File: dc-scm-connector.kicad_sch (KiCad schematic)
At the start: 10 parts, among them J1 Socket_Amphenol_ME10168134011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

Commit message: [#93514] Propagate title and date across all of the sheets
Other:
- title: DC-SCM Carrier Card for OSM-L SoMs -> Datacenter Secure Control Module Breakout Board
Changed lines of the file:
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@@
 	(paper "A3")
 	(title_block
-		(title "DC-SCM Carrier Card for OSM-L SoMs")
-		(date "2025-10-14")
-		(rev "1.1.0")
+		(title "Datacenter Secure Control Module Breakout Board")
+		(date "2021-12-16")
+		(rev "2.0.0")
 	)
 	(bus_alias "DP"

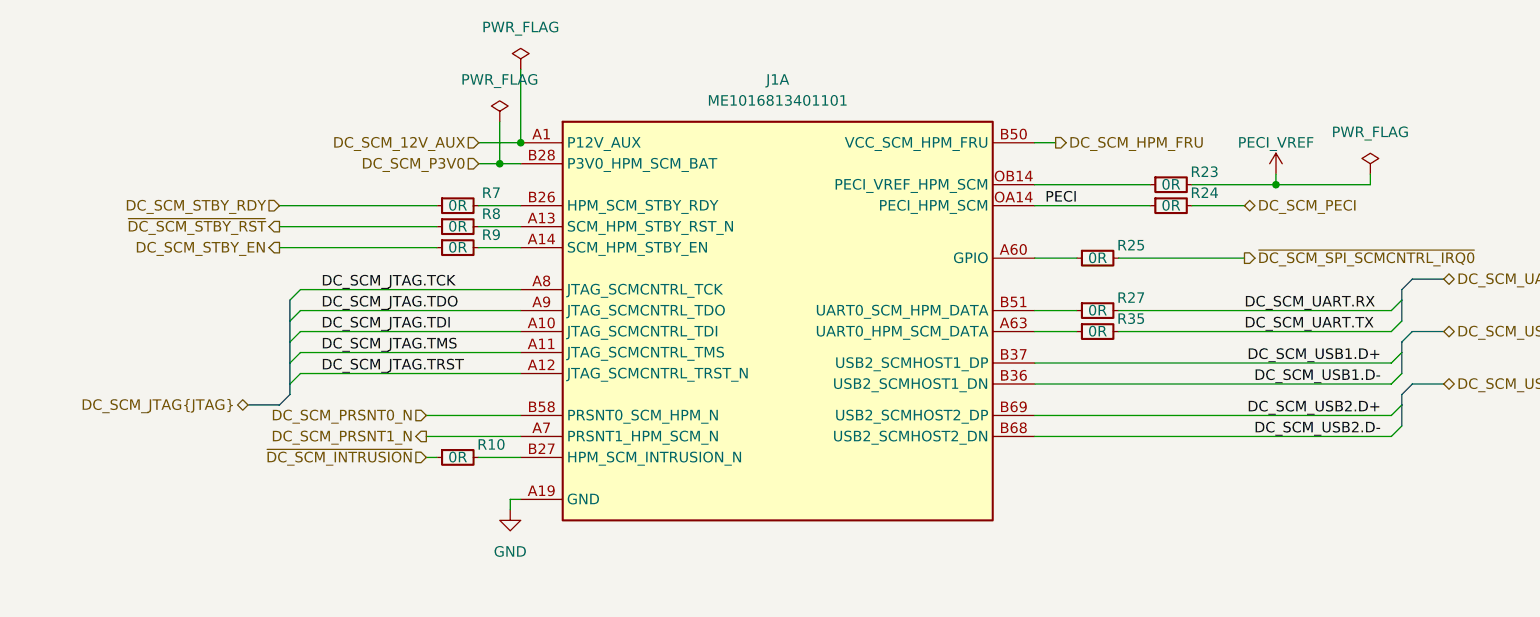
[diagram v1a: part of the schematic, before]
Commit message: [#93514] Align items to grid, add NC-SI testpads
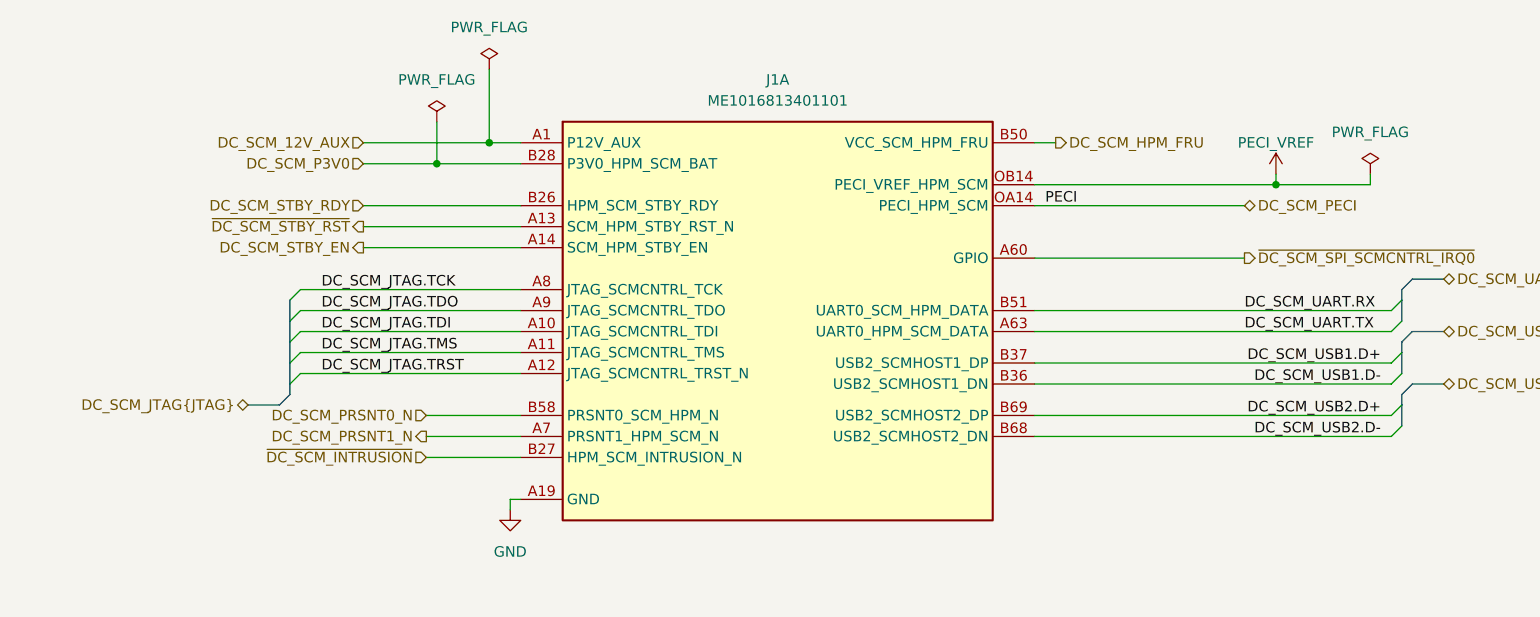
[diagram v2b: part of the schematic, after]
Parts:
- removed R10, R23, R24, R25, R27, R35, R7, R8, R9: R_0R_0402, antmicro-footprints:R_0402_1005Metric, symbol antmicroResistors0402:R_0R_0402
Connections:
- net PECI is gone; now on net DC_SCM_PECI: J1.OA14 (PECI_HPM_SCM)
- net DC_SCM_STBY_EN: now also J1.A14 (SCM_HPM_STBY_EN)
- net DC_SCM_STBY_RDY: now also J1.B26 (HPM_SCM_STBY_RDY)
- net DC_SCM_UART.RX: now also J1.B51 (UART0_SCM_HPM_DATA)
- net DC_SCM_UART.TX: now also J1.A63 (UART0_HPM_SCM_DATA)
- net PECI_VREF: now also J1.OB14 (PECI_VREF_HPM_SCM)
- net ~{DC_SCM_INTRUSION}: now also J1.B27 (HPM_SCM_INTRUSION_N)
- net ~{DC_SCM_SPI_SCMCNTRL_IRQ0}: now also J1.A60 (GPIO)
- net ~{DC_SCM_STBY_RST}: now also J1.A13 (SCM_HPM_STBY_RST_N)

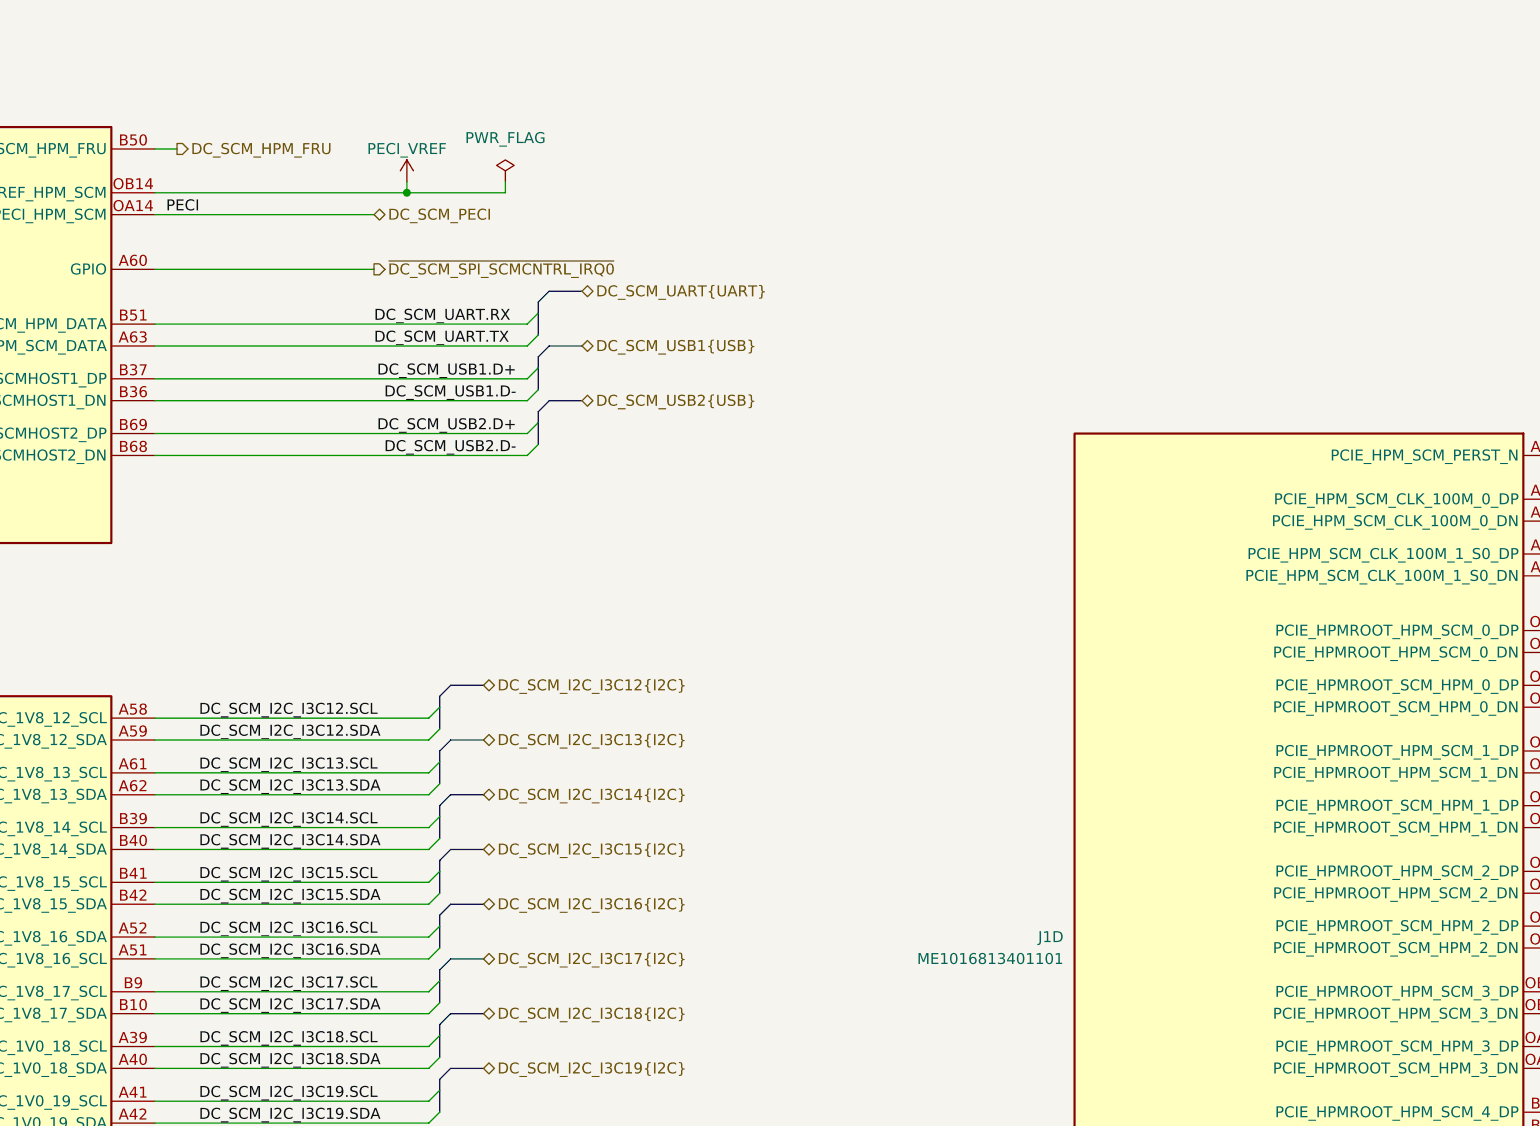
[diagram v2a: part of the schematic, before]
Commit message: [#93514] Replace DC-SCM Socket with newer Value, remove PECI labels
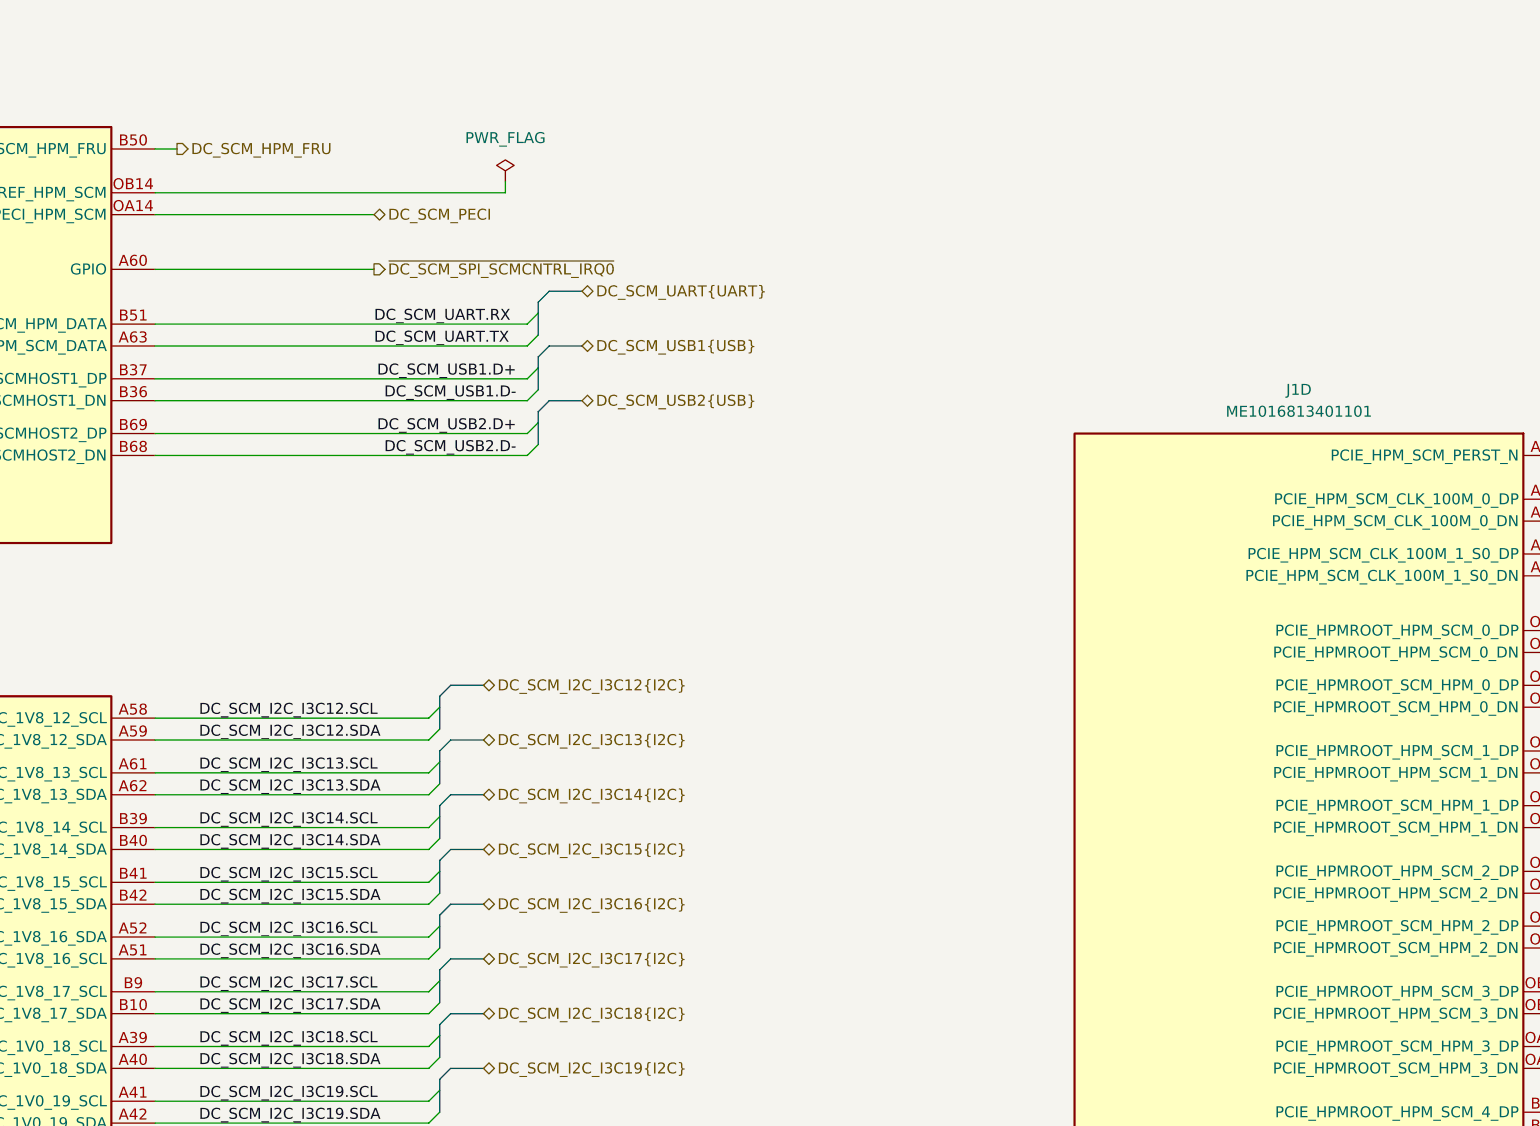
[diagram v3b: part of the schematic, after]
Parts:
- removed J1: Socket_Amphenol_ME1016813401101, antmicro-footprints:Socket_DC-SCM-2.1_2x84_Rev-1-1, symbol antmicroEdgeConnectors:Socket_DC-SCM-2.1_2x84_Rev-1-1
- added J1: Socket_DC-SCM-2.1_2x84_Rev-1-1_CUSTOM, antmicro-footprints:Socket_DC-SCM-2.1_2x84_Rev-1-1, symbol antmicroEdgeConnectors:Socket_DC-SCM-2.1_2x84_Rev-1-1_CUSTOM
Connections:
- net DC-SCM_CLK_100M_0.CLK+: now also J1.A37 (PCIE_HPM_SCM_CLK_100M_0_DP)
- net DC-SCM_CLK_100M_0.CLK-: now also J1.A36 (PCIE_HPM_SCM_CLK_100M_0_DN)
- net DC-SCM_CLK_100M_1.CLK+: now also J1.A69 (PCIE_HPM_SCM_CLK_100M_1_S0_DP)
- net DC-SCM_CLK_100M_1.CLK-: now also J1.A68 (PCIE_HPM_SCM_CLK_100M_1_S0_DN)
- net DC-SCM_PCIE0_SGMII.RX0+: now also J1.OA3 (PCIE_HPMROOT_SCM_HPM_0_DP)
- net DC-SCM_PCIE0_SGMII.RX0-: now also J1.OA2 (PCIE_HPMROOT_SCM_HPM_0_DN)
- net DC-SCM_PCIE0_SGMII.RX1+: now also J1.OA6 (PCIE_HPMROOT_SCM_HPM_1_DP)
- net DC-SCM_PCIE0_SGMII.RX1-: now also J1.OA5 (PCIE_HPMROOT_SCM_HPM_1_DN)
- net DC-SCM_PCIE0_SGMII.RX2+: now also J1.OA9 (PCIE_HPMROOT_SCM_HPM_2_DP)
- net DC-SCM_PCIE0_SGMII.RX2-: now also J1.OA8 (PCIE_HPMROOT_SCM_HPM_2_DN)
- net DC-SCM_PCIE0_SGMII.RX3+: now also J1.OA12 (PCIE_HPMROOT_SCM_HPM_3_DP)
- net DC-SCM_PCIE0_SGMII.RX3-: now also J1.OA11 (PCIE_HPMROOT_SCM_HPM_3_DN)
- net DC-SCM_PCIE0_SGMII.TX0+: now also J1.OB3 (PCIE_HPMROOT_HPM_SCM_0_DP)
- net DC-SCM_PCIE0_SGMII.TX0-: now also J1.OB2 (PCIE_HPMROOT_HPM_SCM_0_DN)
- net DC-SCM_PCIE0_SGMII.TX1+: now also J1.OB6 (PCIE_HPMROOT_HPM_SCM_1_DP)
- net DC-SCM_PCIE0_SGMII.TX1-: now also J1.OB5 (PCIE_HPMROOT_HPM_SCM_1_DN)
- net DC-SCM_PCIE0_SGMII.TX2+: now also J1.OB9 (PCIE_HPMROOT_HPM_SCM_2_DP)
- net DC-SCM_PCIE0_SGMII.TX2-: now also J1.OB8 (PCIE_HPMROOT_HPM_SCM_2_DN)
- net DC-SCM_PCIE0_SGMII.TX3+: now also J1.OB12 (PCIE_HPMROOT_HPM_SCM_3_DP)
- net DC-SCM_PCIE0_SGMII.TX3-: now also J1.OB11 (PCIE_HPMROOT_HPM_SCM_3_DN)
- net DC-SCM_PCIE1.RX0+: now also J1.A31 (PCIE_HPMROOT_SCM_HPM_4_DP)
- net DC-SCM_PCIE1.RX0-: now also J1.A30 (PCIE_HPMROOT_SCM_HPM_4_DN)
- net DC-SCM_PCIE1.TX0+: now also J1.B31 (PCIE_HPMROOT_HPM_SCM_4_DP)
- net DC-SCM_PCIE1.TX0-: now also J1.B30 (PCIE_HPMROOT_HPM_SCM_4_DN)
- net DC-SCM_PCIE_USB_SCMROOT.RX0+: now also J1.A34 (PCIE_SCMROOT_SCM_HPM_DP)
- net DC-SCM_PCIE_USB_SCMROOT.RX0-: now also J1.A33 (PCIE_SCMROOT_SCM_HPM_DN)
- net DC-SCM_PCIE_USB_SCMROOT.TX0+: now also J1.B34 (PCIE_SCMROOT_HPM_SCM_DP)
- net DC-SCM_PCIE_USB_SCMROOT.TX0-: now also J1.B33 (PCIE_SCMROOT_HPM_SCM_DN)
- net DC_SCM_12V_AUX: now also J1.A1 (P12V_AUX), J1.A2 (P12V_AUX), J1.A3 (P12V_AUX), J1.A4 (P12V_AUX)
- net DC_SCM_ESPI.IO0: now also J1.B4 (ESPI_HPMCNTRL_IO_0)
- net DC_SCM_ESPI.IO1: now also J1.B5 (ESPI_HPMCNTRL_IO_1)
- net DC_SCM_ESPI.IO2: now also J1.B6 (ESPI_HPMCNTRL_IO_2)
- net DC_SCM_ESPI.IO3: now also J1.B7 (ESPI_HPMCNTRL_IO_3)
- net DC_SCM_ESPI.SCK: now also J1.B1 (ESPI_HPMCNTRL_CLK)
- net DC_SCM_ESPI.~{ALERT0}: now also J1.B8 (ESPI_HPMCNTRL_ALERT0_N)
- net DC_SCM_ESPI.~{CS0}: now also J1.B2 (ESPI_HPMCNTRL_CS0_N)
- net DC_SCM_ESPI.~{RESET}: now also J1.B3 (ESPI_HPMCNTRL_RESET_N)
- net DC_SCM_HPM_FRU: now also J1.B50 (VCC_SCM_HPM_FRU)
- net DC_SCM_I2C0.SCL: now also J1.A15 (I2C_3V3_0_SCL)
- net DC_SCM_I2C0.SDA: now also J1.A16 (I2C_3V3_0_SDA)
- net DC_SCM_I2C1.SCL: now also J1.A17 (I2C_3V3_1_SCL)
- net DC_SCM_I2C1.SDA: now also J1.A18 (I2C_3V3_1_SDA)
- net DC_SCM_I2C2.SCL: now also J1.A26 (I2C_3V3_2_SCL)
- net DC_SCM_I2C2.SDA: now also J1.A27 (I2C_3V3_2_SDA)
- net DC_SCM_I2C3.SCL: now also J1.A43 (I2C_3V3_3_SCL)
- net DC_SCM_I2C3.SDA: now also J1.A44 (I2C_3V3_3_SDA)
- net DC_SCM_I2C4.SCL: now also J1.A45 (I2C_3V3_4_SCL)
- net DC_SCM_I2C4.SDA: now also J1.A46 (I2C_3V3_4_SDA)
- net DC_SCM_I2C5.SCL: now also J1.A47 (I2C_3V3_5_SCL)
- net DC_SCM_I2C5.SDA: now also J1.A48 (I2C_3V3_5_SDA)
- net DC_SCM_I2C6.SCL: now also J1.A49 (I2C_3V3_6_SCL)
- net DC_SCM_I2C6.SDA: now also J1.A50 (I2C_3V3_6_SDA)
- net DC_SCM_I2C7.SCL: now also J1.B52 (I2C_3V3_7_SCL)
- net DC_SCM_I2C7.SDA: now also J1.B53 (I2C_3V3_7_SDA)
- net DC_SCM_I2C8.SCL: now also J1.B54 (I2C_3V3_8_SCL)
- net DC_SCM_I2C8.SDA: now also J1.B55 (I2C_3V3_8_SDA)
- net DC_SCM_I2C9.SCL: now also J1.B56 (I2C_3V3_9_SCL)
- net DC_SCM_I2C9.SDA: now also J1.B57 (I2C_3V3_9_SDA)
- net DC_SCM_I2C_I3C12.SCL: now also J1.A58 (I2C_I3C_1V8_12_SCL)
- net DC_SCM_I2C_I3C12.SDA: now also J1.A59 (I2C_I3C_1V8_12_SDA)
- net DC_SCM_I2C_I3C13.SCL: now also J1.A61 (I2C_I3C_1V8_13_SCL)
- net DC_SCM_I2C_I3C13.SDA: now also J1.A62 (I2C_I3C_1V8_13_SDA)
- net DC_SCM_I2C_I3C14.SCL: now also J1.B39 (I2C_I3C_1V8_14_SCL)
- net DC_SCM_I2C_I3C14.SDA: now also J1.B40 (I2C_I3C_1V8_14_SDA)
- net DC_SCM_I2C_I3C15.SCL: now also J1.B41 (I2C_I3C_1V8_15_SCL)
- net DC_SCM_I2C_I3C15.SDA: now also J1.B42 (I2C_I3C_1V8_15_SDA)
- net DC_SCM_I2C_I3C16.SCL: now also J1.A52 (I2C_I3C_1V8_16_SDA)
- net DC_SCM_I2C_I3C16.SDA: now also J1.A51 (I2C_I3C_1V8_16_SCL)
- net DC_SCM_I2C_I3C17.SCL: now also J1.B9 (I2C_I3C_1V8_17_SCL)
- net DC_SCM_I2C_I3C17.SDA: now also J1.B10 (I2C_I3C_1V8_17_SDA)
- net DC_SCM_I2C_I3C18.SCL: now also J1.A39 (I2C_I3C_1V0_18_SCL)
- net DC_SCM_I2C_I3C18.SDA: now also J1.A40 (I2C_I3C_1V0_18_SDA)
- net DC_SCM_I2C_I3C19.SCL: now also J1.A41 (I2C_I3C_1V0_19_SCL)
- net DC_SCM_I2C_I3C19.SDA: now also J1.A42 (I2C_I3C_1V0_19_SDA)
- net DC_SCM_JTAG.TCK: now also J1.A8 (JTAG_SCMCNTRL_TCK)
- net DC_SCM_JTAG.TDI: now also J1.A10 (JTAG_SCMCNTRL_TDI)
- net DC_SCM_JTAG.TDO: now also J1.A9 (JTAG_SCMCNTRL_TDO)
- net DC_SCM_JTAG.TMS: now also J1.A11 (JTAG_SCMCNTRL_TMS)
- net DC_SCM_JTAG.TRST: now also J1.A12 (JTAG_SCMCNTRL_TRST_N)
- net DC_SCM_LTPI.RXCK+: now also J1.B24 (LTPI_HPM_SCM_CLK_DP)
- net DC_SCM_LTPI.RXCK-: now also J1.B23 (LTPI_HPM_SCM_CLK_DN)
- net DC_SCM_LTPI.RXD+: now also J1.B21 (LTPI_HPM_SCM_DATA_DP)
- net DC_SCM_LTPI.RXD-: now also J1.B20 (LTPI_HPM_SCM_DATA_DN)
- net DC_SCM_LTPI.TXCK+: now also J1.A24 (LTPI_SCM_HPM_CLK_DP)
- net DC_SCM_LTPI.TXCK-: now also J1.A23 (LTPI_SCM_HPM_CLK_DN)
- net DC_SCM_LTPI.TXD+: now also J1.A21 (LTPI_SCM_HPM_DATA_DP)
- net DC_SCM_LTPI.TXD-: now also J1.A20 (LTPI_SCM_HPM_DATA_DN)
- net DC_SCM_NC-SI.CRS_DV: now also J1.B44 (NCSI_HPM_SCM_CRS_DV)
- net DC_SCM_NC-SI.REF_CLK: now also J1.B43 (NCSI_HPM_SCM_CLK)
- net DC_SCM_NC-SI.RXD0: now also J1.B48 (NCSI_HPM_SCM_D0)
- net DC_SCM_NC-SI.RXD1: now also J1.B49 (NCSI_HPM_SCM_D1)
- net DC_SCM_NC-SI.TXD0: now also J1.B46 (NCSI_SCM_HPM_D0)
- net DC_SCM_NC-SI.TXD1: now also J1.B47 (NCSI_SCM_HPM_D1)
- net DC_SCM_NC-SI.TX_EN: now also J1.B45 (NCSI_SCM_HPM_TX_EN)
- net DC_SCM_P3V0: now also J1.B28 (P3V0_HPM_SCM_BAT)
- net DC_SCM_PECI: now also J1.OA14 (PECI_HPM_SCM)
- net DC_SCM_PRSNT0_N: now also J1.B58 (PRSNT0_SCM_HPM_N)
- net DC_SCM_PRSNT1_N: now also J1.A7 (PRSNT1_HPM_SCM_N)
- net DC_SCM_QSPI.IO0: now also J1.B14 (QSPI_HPMCNTRL_IO_0)
- net DC_SCM_QSPI.IO1: now also J1.B15 (QSPI_HPMCNTRL_IO_1)
- net DC_SCM_QSPI.IO2: now also J1.B16 (QSPI_HPMCNTRL_IO_2)
- net DC_SCM_QSPI.IO3: now also J1.B17 (QSPI_HPMCNTRL_IO_3)
- net DC_SCM_QSPI.SCK: now also J1.B12 (QSPI_HPMCNTRL_CLK)
- net DC_SCM_QSPI.~{CS0}: now also J1.B13 (QSPI_HPMCNTRL_CS0_N)
- net DC_SCM_QSPI.~{CS1}: now also J1.B18 (QSPI_HPMCNTRL_CS1_N)
- net DC_SCM_SPI_SCMCNTRL.DI: now also J1.B62 (SPI_SCMCNTRL_DI_IO0)
- net DC_SCM_SPI_SCMCNTRL.DO: now also J1.B61 (SPI_SCMCNTRL_DO_IO1)
- net DC_SCM_SPI_SCMCNTRL.SCK: now also J1.B60 (SPI_SCMCNTRL_CLK)
- net DC_SCM_SPI_SCMCNTRL.~{CS0}: now also J1.B63 (SPI_SCMCNTRL_CS0_N)
- net DC_SCM_SPI_SCMCNTRL.~{CS1}: now also J1.B59 (SPI_SCMCNTRL_CS1_N)
- net DC_SCM_STBY_EN: now also J1.A14 (SCM_HPM_STBY_EN)
- net DC_SCM_STBY_RDY: now also J1.B26 (HPM_SCM_STBY_RDY)
- net DC_SCM_TPM_SPI.DI: now also J1.A56 (SPI_HPMCNTRL_TPM_DI_IO0)
- net DC_SCM_TPM_SPI.DO: now also J1.A57 (SPI_HPMCNTRL_TPM_DO_IO1)
- net DC_SCM_TPM_SPI.SCK: now also J1.A54 (SPI_HPMCNTRL_TPM_CLK)
- net DC_SCM_TPM_SPI.~{CS0}: now also J1.A55 (SPI_HPMCNTRL_TPM_CS_N)
- net DC_SCM_UART.RX: now also J1.B51 (UART0_SCM_HPM_DATA)
- net DC_SCM_UART.TX: now also J1.A63 (UART0_HPM_SCM_DATA)
- net DC_SCM_USB1.D+: now also J1.B37 (USB2_SCMHOST1_DP)
- net DC_SCM_USB1.D-: now also J1.B36 (USB2_SCMHOST1_DN)
- net DC_SCM_USB2.D+: now also J1.B69 (USB2_SCMHOST2_DP)
- net DC_SCM_USB2.D-: now also J1.B68 (USB2_SCMHOST2_DN)
- net GND: now also J1.A19 (GND), J1.A22 (GND), J1.A25 (GND), J1.A29 (GND), J1.A32 (GND), J1.A35 (GND), J1.A38 (GND), J1.A5 (GND), J1.A53 (GND), J1.A6 (GND), J1.A64 (GND), J1.A67 (GND), J1.A70 (GND), J1.B11 (GND), J1.B19 (GND), J1.B22 (GND), J1.B25 (GND), J1.B29 (GND), J1.B32 (GND), J1.B35 (GND), J1.B38 (GND), J1.B64 (GND), J1.B67 (GND), J1.B70 (GND), J1.OA1 (GND), J1.OA10 (GND), J1.OA13 (GND), J1.OA4 (GND), J1.OA7 (GND), J1.OB1 (GND), J1.OB10 (GND), J1.OB13 (GND), J1.OB4 (GND), J1.OB7 (GND)
- net ~{DC_SCM_INTRUSION}: now also J1.B27 (HPM_SCM_INTRUSION_N)
- net ~{DC_SCM_SPI_SCMCNTRL_IRQ0}: now also J1.A60 (GPIO)
- net ~{DC_SCM_STBY_RST}: now also J1.A13 (SCM_HPM_STBY_RST_N)
- net ~{PCIE_HPM_SCM_PERST}: now also J1.A28 (PCIE_HPM_SCM_PERST_N)

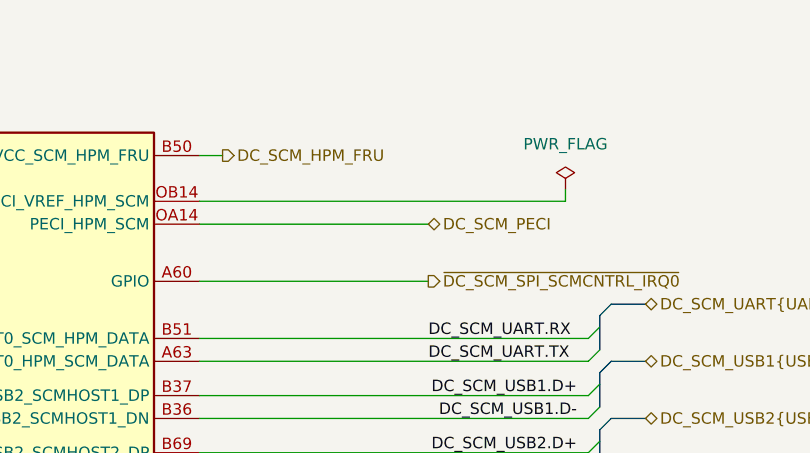
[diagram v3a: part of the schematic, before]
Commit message: [#93514] Add no connect to PECI
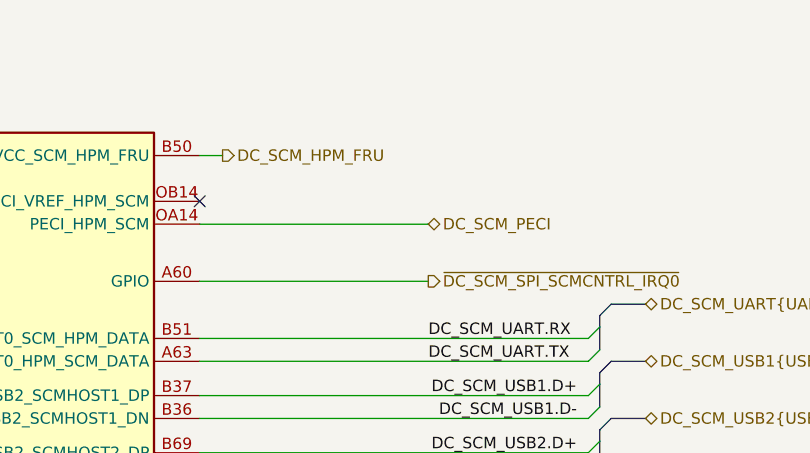
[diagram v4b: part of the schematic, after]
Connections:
- no-connect marks 4 -> 5
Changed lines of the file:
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@@
 	)
 	(no_connect
+		(at 147.32 49.53)
+	)
+	(no_connect
 		(at 311.15 172.72)
 	)
@@
 		)
 	)
-	(wire
-		(pts
-			(xy 187.96 48.26) (xy 187.96 49.53)
-		)
-		(stroke
-			(width 0)
-			(type default)
-		)
-	)
 	(bus
 		(pts
@@
 	(wire
 		(pts
-			(xy 147.32 49.53) (xy 187.96 49.53)
-		)
-		(stroke
-			(width 0)
-			(type default)
-		)
-	)
-	(wire
-		(pts
 			(xy 147.32 219.71) (xy 171.45 219.71)
 		)
@@
 					(unit 1)
 				)
-			)
-		)
-	)
-	(symbol
-		(lib_name "PWR_FLAG_1")
-		(lib_id "antmicropower:PWR_FLAG")
-		(at 187.96 48.26 0)
-		(unit 1)
-		(exclude_from_sim no)
-		(in_bom yes)
-		(on_board yes)
-		(dnp no)
-		(fields_autoplaced yes)
-		(property "Reference" "#FLG01"
-			(at 187.96 46.355 0)
-			(effects
-				(font
-					(size 1.27 1.27)
-				)
-				(hide yes)
-			)
-		)
-		(property "Value" "PWR_FLAG"
-			(at 187.96 43.18 0)
-			(effects
-				(font
-					(size 1.27 1.27)
-				)
-			)
-		)
-		(property "Footprint" ""
-			(at 187.96 48.26 0)
-			(effects
-				(font
-					(size 1.27 1.27)
-				)
-				(hide yes)
-			)
-		)
-		(property "Datasheet" ""
-			(at 187.96 48.26 0)
-			(effects
-				(font
-					(size 1.27 1.27)
-				)
-				(hide yes)
-			)
-		)
-		(property "Description" ""
-			(at 187.96 50.8 0)
-			(effects
-				(font
-					(size 1.27 1.27)
-				)
-				(justify left bottom)
-				(hide yes)
-			)
-		)
-		(pin "1"
-		)
-		(instances
-			(project "bmc-breakout-board"
-				(path "/5d67ef28-5805-4f87-b722-2926dabf7f6e/bae8cef5-57a9-4ec0-acbe-6dac48c5cdf5"
-					(reference "#FLG01")
-					(unit 1)
-				)
